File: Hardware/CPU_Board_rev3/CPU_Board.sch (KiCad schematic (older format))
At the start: 118 parts, among them P1 CONN_01X02, P10 CONN_01X02, P11 CONN_01X06, P12 CONN_01X03, P13 CONN_01X01, P14 CONN_01X03, P15 CONN_01X01, P16 CONN_01X01, P17 CONN_01X01, P18 CONN_01X03, P19 CONN_01X01, P2 USB_B, P20 CONN_01X01, P21 CONN_01X06, P22 CONN_01X01, P23 CONN_01X01, P24 CONN_01X06, P25 CONN_01X04, P26 CONN_01X04, P3 CONN_01X04, P4 CONN_01X04, P5 CONN_01X06, P6 CONN_02X12, P7 CONN_01X02, P8 CONN_01X02, P9 CONN_01X02, Q1 Q_PMOS_GSD, Q2 Q_PNP_BCE, Q3 Q_PNP_BCE, U1 STM32F411RETx, U10 MCDTS2-4N, U11 LPS22HB, U12 INA128, U2 NCP1117DT12G, U3 FT232RL, U4 HTS221, U5 INA128, U6 SPBTLE-RF, U7 A2235-H, U8 LSM303AGR, U9 LSM6DSL, Y1 8MHz

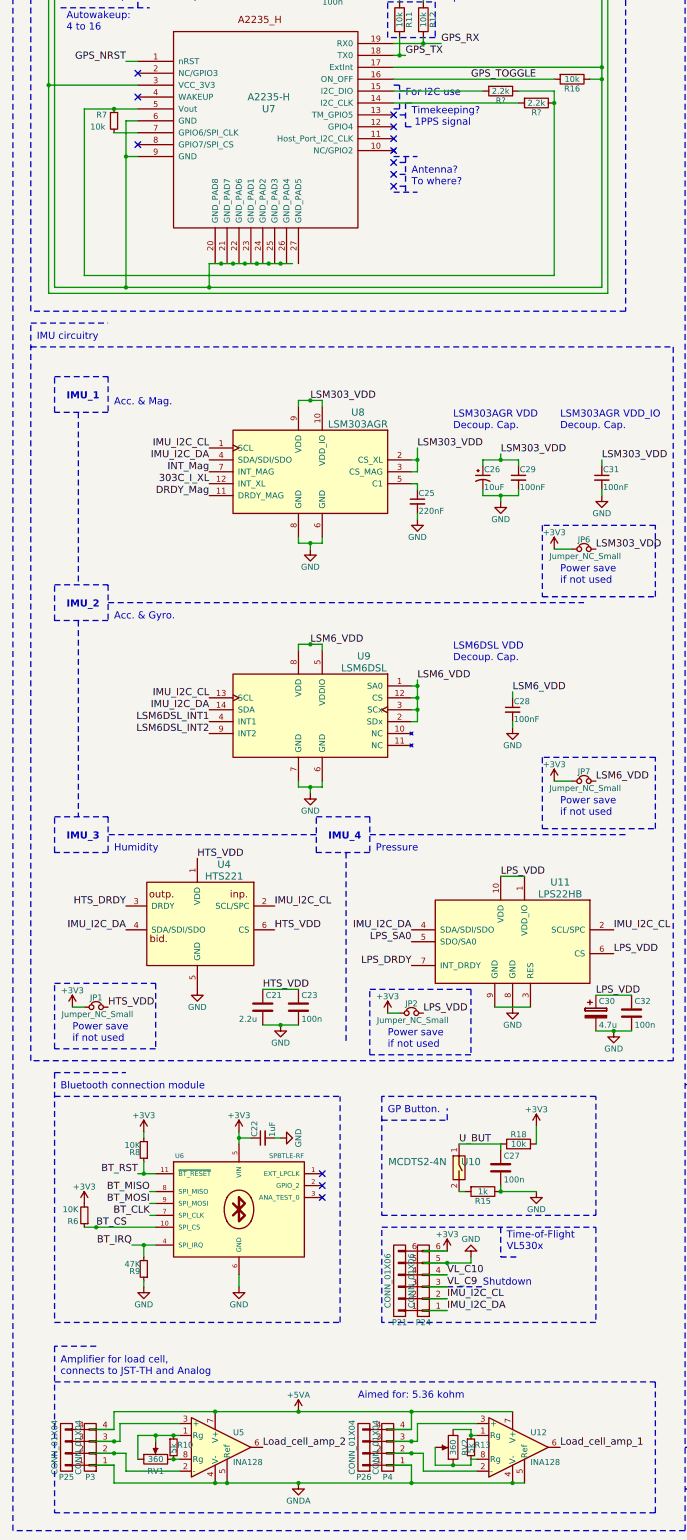
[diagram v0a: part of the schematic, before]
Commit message: Schematic merge and pcb layout fixes
All minor bugs now fixed, Next up is Footprint and library errors,
followed by actual improvements.
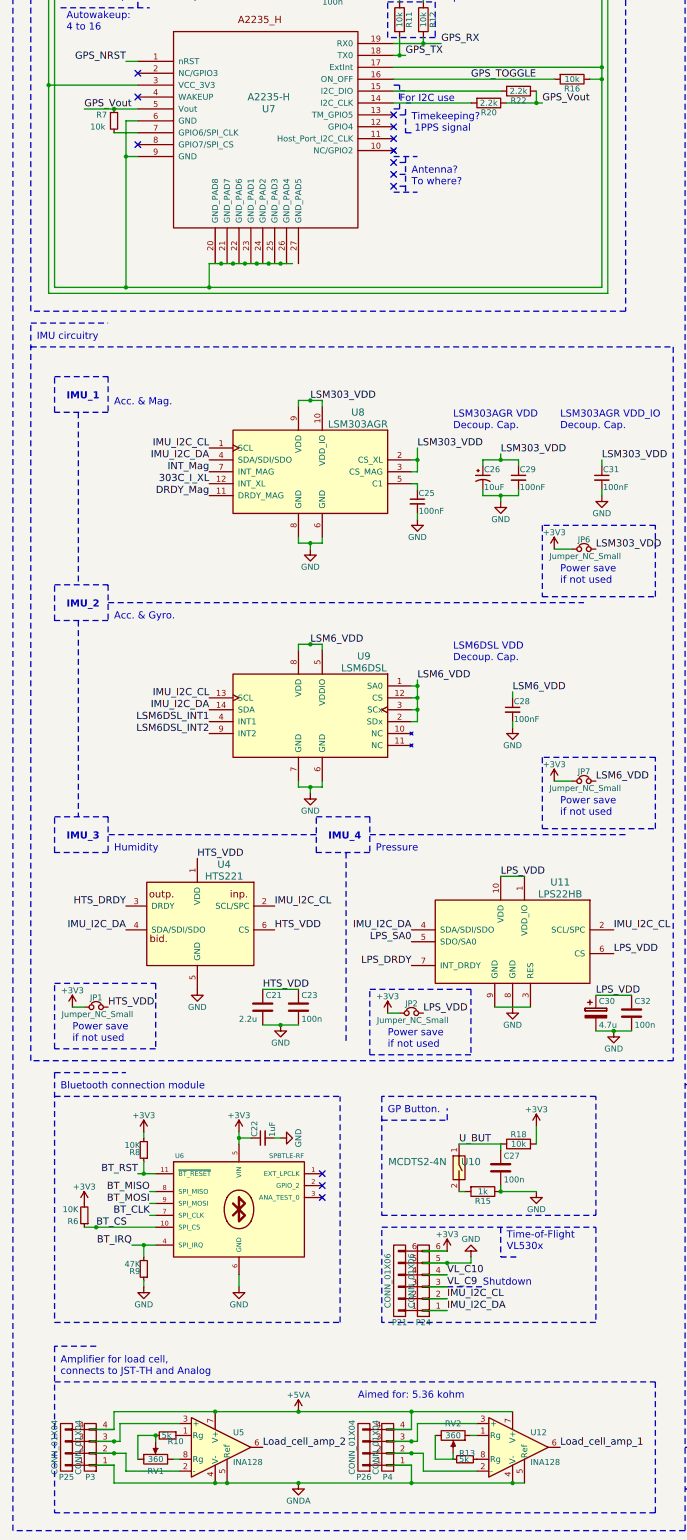
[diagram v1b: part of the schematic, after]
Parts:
- C25: value 220nF -> 100nF
- gave numbers to parts that had none: 2
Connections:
- net GPS_Vout: now reaches R20.1, R22.1, R7.1, U7.5 (Vout)
- net at R10.1, U5.1 (Rg): no longer RV1.1, RV1.2
- net at RV1.3, U5.8 (Rg): no longer R10.2
- net at R13.2, RV2.2: now also RV2.3; no longer RV2.1, U12.8 (Rg)
- new net: RV2.1, U12.1 (Rg)
- new net: R13.1, U12.8 (Rg)
- new net: R10.2, RV1.1, RV1.2
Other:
- moved on the sheet: R10, R13, R20, R22, RV2
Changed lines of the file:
@@
 LIBS:power
 LIBS:device
+LIBS:transistors
+LIBS:conn
 LIBS:linear
 LIBS:regul
+LIBS:74xx
+LIBS:cmos4000
 LIBS:adc-dac
 LIBS:memory
@@
 LIBS:digital-audio
 LIBS:philips
+LIBS:display
 LIBS:cypress
 LIBS:siliconi
@@
 LIBS:atmel
 LIBS:contrib
+LIBS:valves
+LIBS:a2235-h
 LIBS:MOSFET_depleted
 LIBS:misc_rfcom
@@
 NoConn ~ 12150 3400
 NoConn ~ 12150 3300
-Text Notes 12300 3300 0    60   ~ 0
+Text Notes 12300 3350 0    60   ~ 0
 Timekeeping?\n 1PPS signal
 NoConn ~ 12150 3200
-Text Notes 12250 3050 0    60   ~ 0
+Text Notes 12200 3100 0    60   ~ 0
 For I2C use
 Text Notes 9150 1700 0    60   ~ 0
@@
 P 12350 6450
 F 0 "C25" H 12360 6520 50  0000 L CNN
-F 1 "220nF" H 12360 6370 50  0000 L CNN
+F 1 "100nF" H 12360 6370 50  0000 L CNN
 F 2 "Capacitors_SMD:C_0805_HandSoldering" H 12350 6450 50  0001 C CNN
 F 3 "" H 12350 6450 50  0001 C CNN
@@
 L R_Small R13
 U 1 1 59EE0085
-P 12800 14400
-F 0 "R13" H 12830 14420 50  0000 L CNN
-F 1 "5k" V 12800 14350 50  0000 L CNN
-F 2 "Resistors_SMD:R_0805_HandSoldering" H 12800 14400 50  0001 C CNN
-F 3 "" H 12800 14400 50  0001 C CNN
-	1    12800 14400
-	1    0    0    -1
-$EndComp
-$Comp
-L POT RV2
-U 1 1 59EE02F1
-P 12650 14400
-F 0 "RV2" V 12550 14400 50  0000 C CNN
-F 1 "360" V 12650 14400 50  0000 C CNN
-F 2 "Potentiometers:Potentiometer_Trimmer_Bourns_PV36W" H 12650 14400 50  0001 C CNN
-F 3 "" H 12650 14400 50  0001 C CNN
-	1    12650 14400
-	-1   0    0    1
+P 12750 14500
+F 0 "R13" V 12700 14450 50  0000 L CNN
+F 1 "5k" V 12750 14450 50  0000 L CNN
+F 2 "Resistors_SMD:R_0805_HandSoldering" H 12750 14500 50  0001 C CNN
+F 3 "" H 12750 14500 50  0001 C CNN
+	1    12750 14500
+	0    1    1    0
 $EndComp
 $Comp
 L R_Small R10
 U 1 1 59EE4BA3
-P 10300 14400
-F 0 "R10" H 10330 14420 50  0000 L CNN
-F 1 "5k" V 10300 14350 50  0000 L CNN
-F 2 "Resistors_SMD:R_0805_HandSoldering" H 10300 14400 50  0001 C CNN
-F 3 "" H 10300 14400 50  0001 C CNN
-	1    10300 14400
-	1    0    0    -1
+P 10250 14300
+F 0 "R10" V 10300 14300 50  0000 L CNN
+F 1 "5k" V 10250 14250 50  0000 L CNN
+F 2 "Resistors_SMD:R_0805_HandSoldering" H 10250 14300 50  0001 C CNN
+F 3 "" H 10250 14300 50  0001 C CNN
+	1    10250 14300
+	0    1    1    0
 $EndComp
 $Comp
@@
 	12150 3150 12200 3150
 Wire Notes Line
-	12250 3300 12300 3300
+	12250 3350 12300 3350
 Wire Notes Line
 	12250 3200 12200 3200
 Wire Notes Line
-	12250 3100 12250 3300
+	12250 3150 12250 3350
 Wire Notes Line
 	12300 3100 12250 3100
@@
 Connection ~ 11350 14700
 Connection ~ 11350 14100
-Connection ~ 12800 14300
 Wire Wire Line
 	9600 14450 9900 14450
-Connection ~ 10300 14300
-Connection ~ 10300 14500
 Wire Notes Line
 	12600 13050 12900 13050
@@
 	10300 14500 10350 14500
 Wire Wire Line
-	10000 14300 10350 14300
-Wire Wire Line
 	10150 14300 10150 14350
 Wire Wire Line
@@
 Connection ~ 10150 14300
 Wire Wire Line
-	12800 14500 12850 14500
-Wire Wire Line
-	12650 14250 12800 14250
-Wire Wire Line
-	12800 14250 12800 14300
-Wire Wire Line
-	12800 14300 12850 14300
-Wire Wire Line
-	12800 14550 12800 14500
-Wire Wire Line
-	12500 14550 12800 14550
-Wire Wire Line
-	12500 14550 12500 14400
-Connection ~ 12650 14550
-Wire Wire Line
 	3400 7250 4050 7250
 Wire Wire Line
@@
 	1    0    0    -1
 $EndComp
-Wire Wire Line
-	9550 3150 9550 4550
-Wire Wire Line
-	9550 4550 13500 4550
 Connection ~ 9800 3150
 $Comp
-L R R?
+L R R22
 U 1 1 5A18D583
-P 13050 3000
-F 0 "R?" V 13130 3000 50  0000 C CNN
-F 1 "2.2k" V 13050 3000 50  0000 C CNN
-F 2 "Resistors_SMD:R_0805_HandSoldering" V 12980 3000 50  0001 C CNN
-F 3 "" H 13050 3000 50  0001 C CNN
-	1    13050 3000
+P 13200 3000
+F 0 "R22" V 13280 3000 50  0000 C CNN
+F 1 "2.2k" V 13200 3000 50  0000 C CNN
+F 2 "Resistors_SMD:R_0805_HandSoldering" V 13130 3000 50  0001 C CNN
+F 3 "" H 13200 3000 50  0001 C CNN
+	1    13200 3000
 	0    1    1    0
 $EndComp
 $Comp
-L R R?
+L R R20
 U 1 1 5A18E2EE
-P 13350 3100
-F 0 "R?" V 13430 3100 50  0000 C CNN
-F 1 "2.2k" V 13350 3100 50  0000 C CNN
-F 2 "Resistors_SMD:R_0805_HandSoldering" V 13280 3100 50  0001 C CNN
-F 3 "" H 13350 3100 50  0001 C CNN
-	1    13350 3100
+P 12950 3100
+F 0 "R20" V 13030 3100 50  0000 C CNN
+F 1 "2.2k" V 12950 3100 50  0000 C CNN
+F 2 "Resistors_SMD:R_0805_HandSoldering" V 12880 3100 50  0001 C CNN
+F 3 "" H 12950 3100 50  0001 C CNN
+	1    12950 3100
 	0    1    1    0
 $EndComp
 Wire Wire Line
-	13500 4550 13500 3000
-Wire Wire Line
-	13500 3000 13200 3000
-Connection ~ 13500 3100
-Wire Wire Line
 	13900 2900 13800 2900
 Wire Notes Line
 	12200 3150 12200 2950
 Wire Wire Line
-	12900 3000 12150 3000
+	13050 3000 12150 3000
+Wire Wire Line
+	12800 3100 12150 3100
+Text Label 9550 3150 0    60   ~ 0
+GPS_Vout
+Text Label 13400 3100 0    60   ~ 0
+GPS_Vout
+Wire Wire Line
+	13350 3000 13350 3100
+Wire Wire Line
+	13100 3100 13400 3100
+Connection ~ 13350 3100
+Wire Wire Line
+	12850 14300 12800 14300
+Wire Wire Line
+	12650 14450 12650 14500
+$Comp
+L POT RV2
+U 1 1 59EE02F1
+P 12650 14300
+F 0 "RV2" V 12550 14300 50  0000 C CNN
+F 1 "360" V 12650 14300 50  0000 C CNN
+F 2 "Potentiometers:Potentiometer_Trimmer_Bourns_PV36W" H 12650 14300 50  0001 C CNN
+F 3 "" H 12650 14300 50  0001 C CNN
+	1    12650 14300
+	0    1    1    0
+$EndComp
+Wire Wire Line
+	12500 14300 12500 14500
+Wire Wire Line
+	12500 14500 12650 14500
 Wire Wire Line
-	13200 3100 12150 3100
+	10000 14300 10150 14300
 $EndSCHEMATC

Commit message: Rev 3 (most stuff)
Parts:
- removed C35: 10uF, Capacitors_SMD:CP_Elec_5x5.3, symbol CP1_Small
- removed C36, C37, C39: 100n, Capacitors_SMD:C_0805_HandSoldering, symbol C
- removed C38: 10n, Capacitors_SMD:C_0805_HandSoldering, symbol C
- removed IM1: LSM9DS1, FOOTPRINTS:LGA-24L_3x3.5mm_Pitch0.43mm_Handsolder, symbol LSM9DS1
- removed JP5: Jumper_NC_Small, Pin_Headers:Pin_Header_Straight_1x02_Pitch2.54mm, symbol Jumper_NC_Small
- removed P6: CONN_02X12, Housings_DIP:DIP-24_W15.24mm_Socket, symbol CONN_02X12
- removed R1: 10k, Resistors_SMD:R_0805_HandSoldering, symbol R
- added C31: 100n, Capacitors_SMD:C_0805_HandSoldering, symbol C
- added R18: 1k, Resistors_SMD:R_0805_HandSoldering, symbol R
- added R21: 10k, Resistors_SMD:R_0805_HandSoldering, symbol R
- added U11: MCDTS2-4N, Buttons_Switches_SMD:SW_SPST_PTS645, symbol CHERRY-MX
- R6: renamed from R17; value 10k -> 5k
- R7: renamed from R19; value 10k -> 5k
- U12: renamed from U11; footprint FOOTPRINTS:HLGA-10L -> FOOTPRINTS:HLGA-10L_2x2mm_P.5mm_HS
- U4: footprint FOOTPRINTS:HLGA-6L_2x2x.9mm -> FOOTPRINTS:HLGA-6L_2x2x.9mm_HS
- U8: footprint FOOTPRINTS:LGA-12_2x2mm_Pitch0.5mm_Handsolder -> FOOTPRINTS:LGA-12_2x2mm_P.5mm_HS
- U9: footprint FOOTPRINTS:LGA-14 -> FOOTPRINTS:LGA-14_2.5x3mm_P.5_HS
- renumbered C34 to C10, C13 to C12, C9 to C13, C15 to C14, C17 to C15, C12 to C16, C16 to C17, C14 to C18, C18 to C21, C21 to C22, C22 to C23, C23 to C24, C24 to C25, C25 to C26, C26 to C27, C27 to C30, C30 to C32, C31 to C33, C32 to C34, C33 to C35, C10 to C9, JP3 to JP1, JP4 to JP2, JP1 to JP3, JP2 to JP4, JP6 to JP5, JP7 to JP6, P7 to P10, P8 to P11, P9 to P12, P10 to P13, P11 to P14, P12 to P15, P13 to P16, P14 to P17, P15 to P18, P16 to P19, P17 to P20, P18 to P21, P19 to P22, P20 to P23, P22 to P24, P23 to P25, P25 to P3, P3 to P4, P26 to P5, P4 to P6, P21 to P7, P24 to P8, P5 to P9, R2 to R1, R8 to R10, R9 to R11, R10 to R12, R11 to R13, R12 to R14, R13 to R15, R20 to R16, R15 to R17, R22 to R19, R3 to R2, R18 to R20, R16 to R22, R21 to R23, R4 to R3, R5 to R4, R14 to R5, R6 to R8, R7 to R9, U12 to U13, U3 to U2, U2 to U3
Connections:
- net +3V3: now also R21.2
- net GND: now also C31.2, R18.1
- net GPS_NRST: now also U1.8 (PC0/ADC1_IN10); no longer U1.9 (PC1/ADC1_IN11)
- net GPS_TOGGLE: now also U1.38 (PC7/I2S2_CK/I2S3_MCK/SDIO_D7/SPI2_SCK/TIM3_CH2/USART6_RX); no longer U1.44 (ADC1_EXTI11/SPI4_MISO/TIM1_CH4/USART1_CTS/USART6_TX/USB_OTG_FS_DM/PA11)
- net NRST: now also C31.1, R21.1, U11.1; no longer U1.8 (PC0/ADC1_IN10)
- new net: R18.2, U11.2
- no-connect marks 62 -> 50
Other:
- note added: "NRST Button."
- note removed: "IMU"
- note removed: "IMU Accelerometer/Gyroscope/Magnetometer\n("Backup")"
- moved on the sheet: C30, P7, P8, R17, R20, R6, R7, U10

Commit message: Revision 3 routed and completed
* Schematic completed
* Layout of components complete
* Routing complete
* Excessive via placing complete (All potential antennas, no matter how
slight should have been prevented)
* Gerbers generated
* Drill generated
* A2235 footprint/library fixed
* Minor other adjustments
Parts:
- removed C33: 100nF, Capacitors_SMD:C_0805_HandSoldering, symbol C_Small
- removed JP3, JP4, JP5, JP6: Jumper_NC_Small, Pin_Headers:Pin_Header_Straight_1x02_Pitch2.54mm, symbol Jumper_NC_Small
- removed P13: CONN_01X02, Pin_Headers:Pin_Header_Straight_1x02_Pitch2.54mm, symbol CONN_01X02
- removed P17: CONN_01X03, Pin_Headers:Pin_Header_Straight_1x03_Pitch2.54mm, symbol CONN_01X03
- removed P18: CONN_01X01, Pin_Headers:Pin_Header_Straight_1x01_Pitch2.54mm, symbol CONN_01X01
- removed U8: LSM303AGR, FOOTPRINTS:LGA-12_2x2mm_P.5mm_HS, symbol LSM303Cx
- added P26: CONN_01X04, Connectors_Molex:Molex_KK-6410-04_04x2.54mm_Straight, symbol CONN_01X04
- added Q4, Q5: BSS138, TO_SOT_Packages_SMD:SOT-23, symbol BSS138
- added R24, R25, R26, R27: R, Resistors_SMD:R_0805_HandSoldering, symbol R
- added U8: LSM303AGR, FOOTPRINTS:LGA-12_2x2mm_P.5mm_HS, symbol LSM303AGR
- P2: footprint Connectors:USB_Micro-B -> Connectors:USB_Mini-B
- P8: footprint FOOTPRINTS:JST_PH_S6B-PH-K_06x2.50mm_Angled -> FOOTPRINTS:JST_PH_S6B-PH-K_06x2.54mm_Angled
- R6, R7: value 5k -> 10k
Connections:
- net HTS_VDD is gone; now on net +3V3: C22.1, C24.1, U4.1 (VDD), U4.6 (CS)
- net LPS_VDD is gone; now on net +3V3: C32.1, C34.1, U12.1 (VDD_IO), U12.10 (VDD), U12.6 (CS)
- net LSM303_VDD is gone; now on net +3V3: C27.1, C29.1
- net LSM6_VDD is gone; now on net +3V3: C28.1, U9.1 (SA0), U9.12 (CS), U9.2 (SDx), U9.3 (SCx), U9.5 (VDDIO), U9.8 (VDD)
- net +3V3: now also P7.1 (P1), P8.1 (P1), Q4.1 (G), Q5.1 (G), R26.2, R27.2, U8.10 (VDD_IO), U8.2 (CS_XL), U8.3 (CS_MAG), U8.9 (VDD); no longer P7.6 (P6), P8.6 (P6)
- net GND: now also P7.2 (P2), P8.2 (P2), U7.20 (GND_PAD8), U7.21 (GND_PAD7), U7.22 (GND_PAD6), U7.23 (GND_PAD1), U7.24 (GND_PAD2), U7.25 (GND_PAD3), U7.26 (GND_PAD4), U7.27 (GND_PAD5), P26.4 (P4), U8.6 (GND), U8.8 (GND); no longer P7.5 (P5), P8.5 (P5)
- net IMU_I2C_CL: now also P12.2 (P2), P7.5 (P5), P8.5 (P5), Q4.2 (S), R26.1, U8.1 (SCL); no longer P7.2 (P2), P8.2 (P2)
- net IMU_I2C_DA: now also P12.1 (P1), P7.6 (P6), P8.6 (P6), Q5.2 (S), R27.1, U8.4 (SDA); no longer P7.1 (P1), P8.1 (P1)
- net LSM6DSL_INT1: no longer P12.2 (P2)
- net LSM6DSL_INT2: no longer P12.1 (P1)
- net VL_C10: now also P7.3 (P3), P8.3 (P3); no longer P7.4 (P4), P8.4 (P4)
- net at C26.1: now also U8.5 (C1)
- net 303C_I_XL: no longer names the net of U1.20 (ADC1_IN4/I2S1_WS/I2S3_WS/SPI1_NSS/SPI3_NSS/USART2_CK/PA4)
- net DRDY_Mag: no longer names the net of U1.26 (ADC1_IN8/I2S5_CK/SPI5_SCK/TIM1_CH2N/TIM3_CH3/PB0)
- net INT_Mag: no longer names the net of U1.21 (ADC1_IN5/I2S1_CK/SPI1_SCK/TIM2_CH1/TIM2_ETR/PA5)
- net LPS_DRDY renamed LPS_I_DRDY
- removed net VL_C9: P7.3 (P3), P8.3 (P3), U1.40 (PC9/I2C3_SDA/I2S_CKIN/RCC_MCO_2/SDIO_D1/TIM3_CH4)
- new net: P26.3 (P3), Q4.3 (D), R24.1
- new net: P26.2 (P2), Q5.3 (D), R25.1
- new net INT/DRDY_Mag: U8.7 (INT_MAG/DRDY)
- new net TOF_SD: P7.4 (P4), P8.4 (P4), U1.40 (PC9/I2C3_SDA/I2S_CKIN/RCC_MCO_2/SDIO_D1/TIM3_CH4)
- new net VBat: P26.1 (P1), R24.2, R25.2
- no-connect marks 50 -> 54
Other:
- note added: "2:\nHumidity"
- note added: "3:\nPressure"
- note added: "Battery level\nLogic level converter"
- note added: "GND\nsCL\nsDA\nVBat"
- note added: "I2C 1"
- note added: "I2C 2"
- note added: "I2C 3"
- note added: "I2C 4"
- note added: "I2C circuitry"
- note added: "Measurement\nNodes I2C\n"
- note removed: "Antenna?\nTo where?"
- note removed: "Humidity"
- note removed: "IMU 1 pins"
- note removed: "IMU 2 interrupt pins"
- note removed: "IMU 3 DRDY pin"
- note removed: "IMU 4 SA0/DRDY pins"
- note removed: "IMU circuitry"
- note removed: "IMU_3"
- note removed: "IMU_4"
- note removed: "LSM303AGR VDD_IO\nDecoup. Cap."
- note removed: "Measurement\nNodes IMU\n"
- note removed: "Pressure"
- note removed: "Shutdown"
- note removed: "Timekeeping?\n 1PPS signal"
- moved on the sheet: C22, C23, C24, C25, C26, C27, C28, C29, C30, C31, C32, C34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

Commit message: last fixes
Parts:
- U13, U5: footprint Housings_SOIC:SO-8_5.3x6.2mm_Pitch1.27mm -> Housings_SOIC:SOIC-8_3.9x4.9mm_Pitch1.27mm
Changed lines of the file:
@@
 F 0 "U5" H 16600 12925 50  0000 L CNN
 F 1 "INA128" H 16600 12675 50  0000 L CNN
-F 2 "Housings_SOIC:SO-8_5.3x6.2mm_Pitch1.27mm" H 16550 12800 50  0001 C CNN
+F 2 "Housings_SOIC:SOIC-8_3.9x4.9mm_Pitch1.27mm" H 16550 12800 50  0001 C CNN
 F 3 "" H 16550 12800 50  0001 C CNN
 	1    16450 12800
@@
 F 0 "U13" H 19100 12925 50  0000 L CNN
 F 1 "INA128" H 19100 12675 50  0000 L CNN
-F 2 "Housings_SOIC:SO-8_5.3x6.2mm_Pitch1.27mm" H 19050 12800 50  0001 C CNN
+F 2 "Housings_SOIC:SOIC-8_3.9x4.9mm_Pitch1.27mm" H 19050 12800 50  0001 C CNN
 F 3 "" H 19050 12800 50  0001 C CNN
 	1    18950 12800
@@
 	13900 10800 13900 13400
 Wire Wire Line
-	9500 13400 13900 13400
+	13900 13400 9500 13400
 Wire Wire Line
 	9500 13400 9500 10800

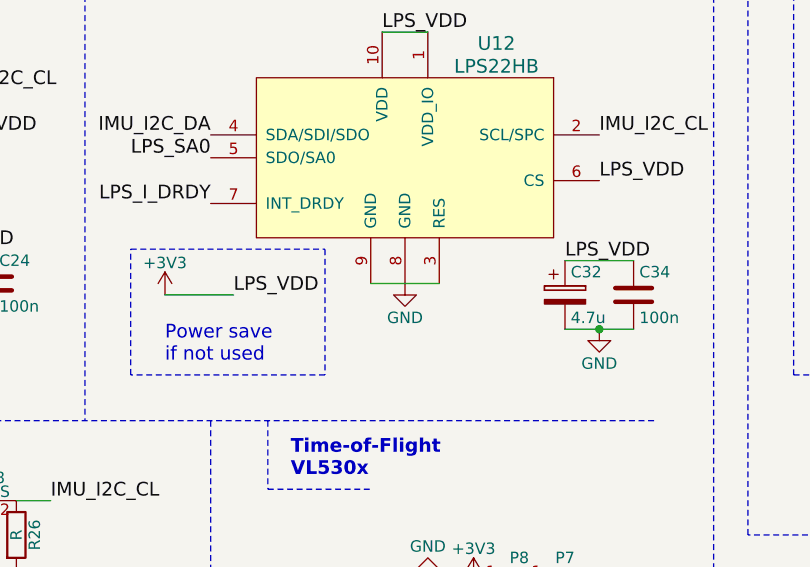
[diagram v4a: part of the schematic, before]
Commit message: Added appendix to report, fixed last error in pcb layout (missing junction)
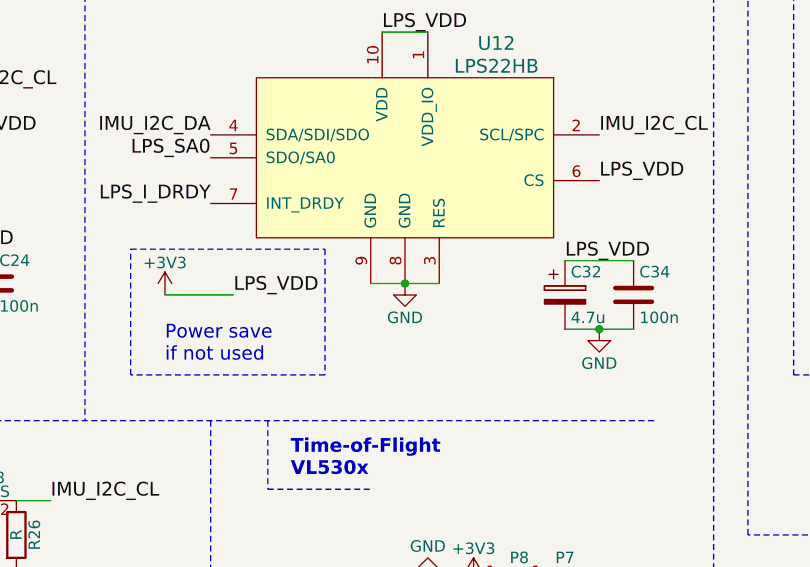
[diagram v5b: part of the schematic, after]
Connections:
- net GND: now also U12.3 (RES), U12.9 (GND)
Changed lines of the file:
@@
 Wire Notes Line
 	14600 8200 14600 1250
+Connection ~ 13100 7100
 $EndSCHEMATC
